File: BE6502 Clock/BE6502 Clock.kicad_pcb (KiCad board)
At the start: 2 copper layers, 45.7 x 99.1 mm, 28 parts, among them J1 CLOCK_SEL, M1 Mounting, M2 Mounting, M3 Mounting, M4 Mounting, SW1 MANUAL, SW2 CLK_SEL, U1 LM555, U2 LM555, U3 LM555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

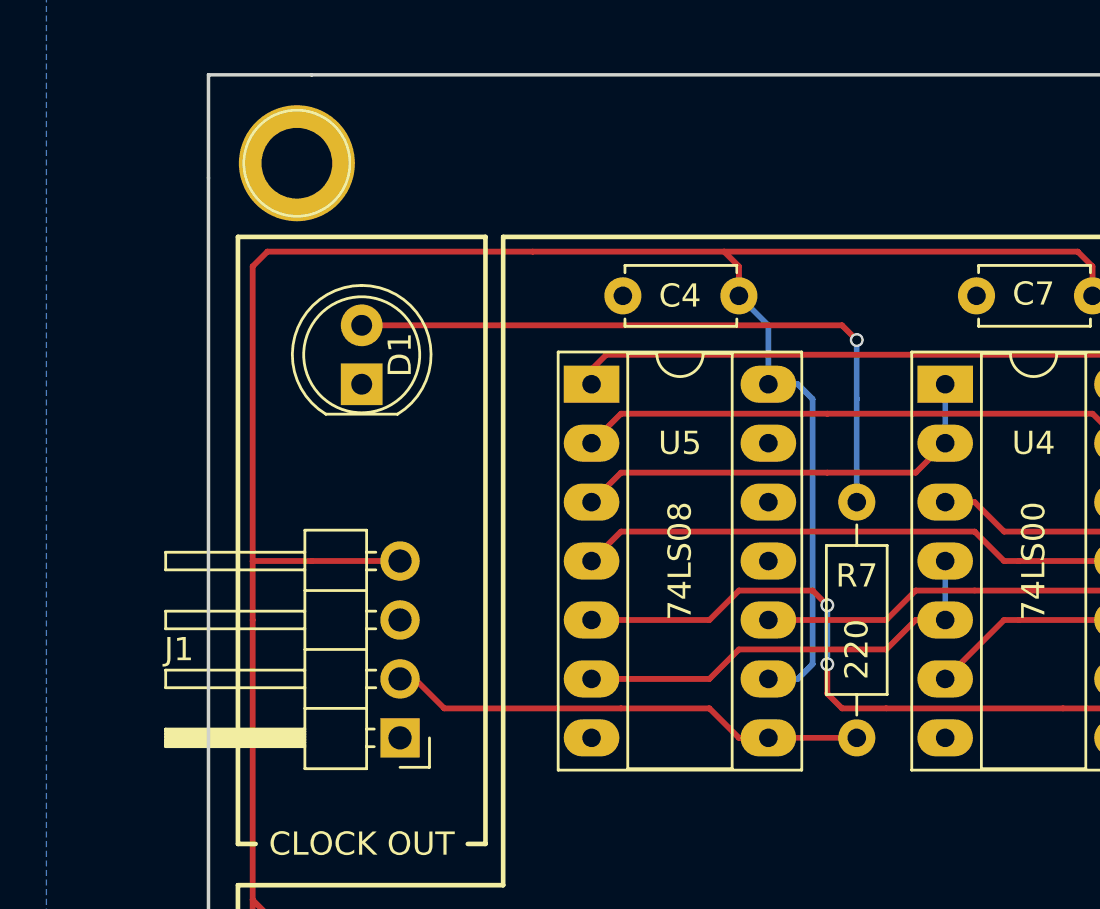
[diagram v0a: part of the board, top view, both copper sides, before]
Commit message: Adjusted clock module after building
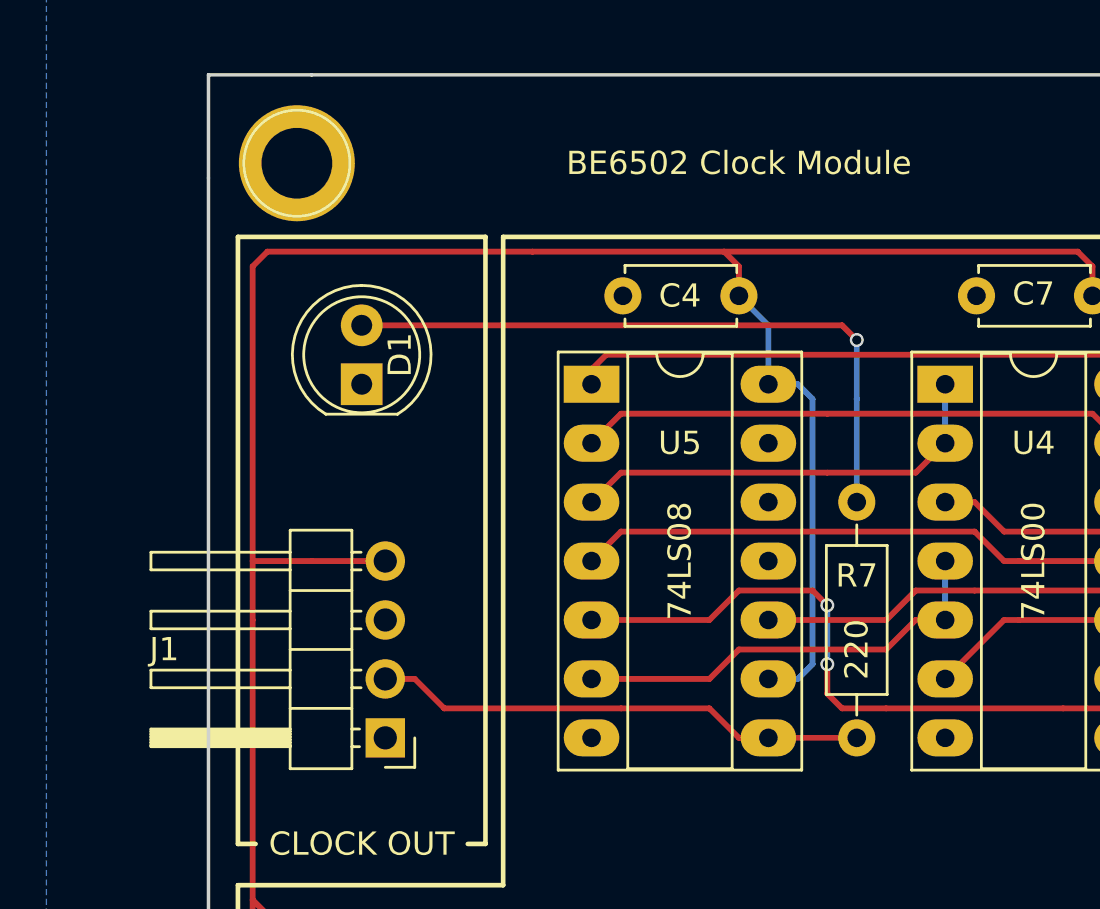
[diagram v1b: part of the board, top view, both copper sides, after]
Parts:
- moved J1 0.63 mm to (132.7, 85.7)
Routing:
- net VCC: track 290.6 -> 290.0 mm
- net CLOCK_OUT: track 20.7 -> 21.4 mm
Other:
- board text added: "555 TIMER"
- board text added: "ADJUSTABLE"
- board text added: "BE6502 Clock Module"
- board text added: "GND"
- board text added: "MANUAL"
- board text added: "NAND GATES"
- board text added: "OUT"
- board text added: "Revision A"
- board text added: "TURN CLOCKWISE TO SLOW CLOCK"
- board text added: "VCC"
- board text added: "github.com/tebl"

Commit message: Updated clock with capacitor from video 3
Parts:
- added C8: 100nF, Capacitors_THT:C_Disc_D4.7mm_W2.5mm_P5.00mm, F.Cu at (129.5, 118.7)
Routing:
- net Net-(C8-Pad1): track 81.5 -> 95.7 mm
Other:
- board text added: "Revision B"
- board text removed: "Revision A"

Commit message: Fixed issue with clock module
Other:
- rule pad_to_mask_clearance: 0.2 -> 0

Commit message: Update errata and bump module revision number
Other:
- board text added: "Revision C"
- board text removed: "Revision B"
